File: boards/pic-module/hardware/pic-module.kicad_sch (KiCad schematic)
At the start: 42 parts, among them J2 ICSP, J20 12V IN, J3 J3 host, J4 J4 host, J5 UART, Q1 SUD50P04-08, U1 PIC32MK1024MCM064-I/PT, U2 MCP1826S-3302E/DB, U20 TDN 5-2411WI, Y1 12MHz

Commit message: Move core, can-card, io-card, serial-card, can-ssr, probe-helper to rev B
Rev A went to PCBWay and is tagged revA. Rev B replaces parts the Mouser
BOM check flagged (obsolete, end of life, not recommended for new designs,
or not orderable) and swaps out-of-stock passives and diodes for in-stock
equivalents. Field-only changes, same footprints, no layout change; the
reference boards (can-controller, pic-module) get the same part numbers.
The rev A order lists (DigiKey, Mouser) carry the same substitutions; the
Mouser list leaves out the T821 box headers (bought from DigiKey).

docs/rev-b-changes.md lists every change and the rev B to-dos (MAX7219 is
obsolete and must be replaced). transfer/mouser-revA.xlsx (Mouser BOM
check) consumed.

Co-Authored-By: Claude Opus 5.5 <noreply@anthropic.com>
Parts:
- C1, C2, C60, C61, C62, C63, C8: MPN GRM31CR71E106KA12L -> CL31B106KAHNNNE; Manufacturer Murata -> Samsung Electro-Mechanics
- C10: MPN GRM31MR71H105KA88L -> C1206C105K5RACTU; Manufacturer Murata -> KEMET
- C11, C12: MPN GRM2165C1H270JA01D -> C0805C270J5GACTU; Manufacturer Murata -> KEMET
- C13, C3, C4, C5, C6, C7, C9: MPN GRM21BR71H104KA01L -> C0805C104K5RACTU; Manufacturer Murata -> KEMET
- D1, D2, D32: MPN LTST-C150GKT -> LTST-C150KGKT
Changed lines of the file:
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@@
 			)
 		)
-		(property "Manufacturer" "Murata"
+		(property "Manufacturer" "Samsung Electro-Mechanics"
 			(at 142.24 68.58 0)
 			(hide yes)
@@
 			)
 		)
-		(property "MPN" "GRM31CR71E106KA12L"
+		(property "MPN" "CL31B106KAHNNNE"
 			(at 142.24 68.58 0)
 			(hide yes)
@@
 			)
 		)
-		(property "Manufacturer" "Murata"
+		(property "Manufacturer" "Samsung Electro-Mechanics"
 			(at 154.94 68.58 0)
 			(hide yes)
@@
 			)
 		)
-		(property "MPN" "GRM31CR71E106KA12L"
+		(property "MPN" "CL31B106KAHNNNE"
 			(at 154.94 68.58 0)
 			(hide yes)
@@
 			)
 		)
-		(property "MPN" "LTST-C150GKT"
+		(property "MPN" "LTST-C150KGKT"
 			(at 180.34 60.96 0)
 			(hide yes)
@@
 			)
 		)
-		(property "Manufacturer" "Murata"
+		(property "Manufacturer" "Samsung Electro-Mechanics"
 			(at 205.74 73.66 0)
 			(hide yes)
@@
 			)
 		)
-		(property "MPN" "GRM31CR71E106KA12L"
+		(property "MPN" "CL31B106KAHNNNE"
 			(at 205.74 73.66 0)
 			(hide yes)
@@
 			)
 		)
-		(property "Manufacturer" "Murata"
+		(property "Manufacturer" "Samsung Electro-Mechanics"
 			(at 254 73.66 0)
 			(hide yes)
@@
 			)
 		)
-		(property "MPN" "GRM31CR71E106KA12L"
+		(property "MPN" "CL31B106KAHNNNE"
 			(at 254 73.66 0)
 			(hide yes)
@@
 			)
 		)
-		(property "Manufacturer" "Murata"
+		(property "Manufacturer" "Samsung Electro-Mechanics"
 			(at 297.18 71.12 0)
 			(hide yes)
@@
 			)
 		)
-		(property "MPN" "GRM31CR71E106KA12L"
+		(property "MPN" "CL31B106KAHNNNE"
 			(at 297.18 71.12 0)
 			(hide yes)
@@
 			)
 		)
-		(property "Manufacturer" "Murata"
+		(property "Manufacturer" "Samsung Electro-Mechanics"
 			(at 335.28 71.12 0)
 			(hide yes)
@@
 			)
 		)
-		(property "MPN" "GRM31CR71E106KA12L"
+		(property "MPN" "CL31B106KAHNNNE"
 			(at 335.28 71.12 0)
 			(hide yes)
@@
 			)
 		)
-		(property "MPN" "LTST-C150GKT"
+		(property "MPN" "LTST-C150KGKT"
 			(at 360.68 60.96 0)
 			(hide yes)
@@
 			)
 		)
-		(property "Manufacturer" "Murata"
+		(property "Manufacturer" "KEMET"
 			(at 25.4 129.54 0)
 			(hide yes)
@@
 			)
 		)
-		(property "MPN" "GRM21BR71H104KA01L"
+		(property "MPN" "C0805C104K5RACTU"
 			(at 25.4 129.54 0)
 			(hide yes)
@@
 			)
 		)
-		(property "Manufacturer" "Murata"
+		(property "Manufacturer" "KEMET"
 			(at 40.64 129.54 0)
 			(hide yes)
@@
 			)
 		)
-		(property "MPN" "GRM21BR71H104KA01L"
+		(property "MPN" "C0805C104K5RACTU"
 			(at 40.64 129.54 0)
 			(hide yes)
@@
 			)
 		)
-		(property "Manufacturer" "Murata"
+		(property "Manufacturer" "KEMET"
 			(at 55.88 129.54 0)
 			(hide yes)
@@
 			)
 		)
-		(property "MPN" "GRM21BR71H104KA01L"
+		(property "MPN" "C0805C104K5RACTU"
 			(at 55.88 129.54 0)
 			(hide yes)
@@
 			)
 		)
-		(property "Manufacturer" "Murata"
+		(property "Manufacturer" "KEMET"
 			(at 71.12 129.54 0)
 			(hide yes)
@@
 			)
 		)
-		(property "MPN" "GRM21BR71H104KA01L"
+		(property "MPN" "C0805C104K5RACTU"
 			(at 71.12 129.54 0)
 			(hide yes)
@@
 			)
 		)
-		(property "Manufacturer" "Murata"
+		(property "Manufacturer" "KEMET"
 			(at 86.36 129.54 0)
 			(hide yes)
@@
 			)
 		)
-		(property "MPN" "GRM21BR71H104KA01L"
+		(property "MPN" "C0805C104K5RACTU"
 			(at 86.36 129.54 0)
 			(hide yes)
@@
 			)
 		)
-		(property "Manufacturer" "Murata"
+		(property "Manufacturer" "Samsung Electro-Mechanics"
 			(at 101.6 129.54 0)
 			(hide yes)
@@
 			)
 		)
-		(property "MPN" "GRM31CR71E106KA12L"
+		(property "MPN" "CL31B106KAHNNNE"
 			(at 101.6 129.54 0)
 			(hide yes)
@@
 			)
 		)
-		(property "Manufacturer" "Murata"
+		(property "Manufacturer" "KEMET"
 			(at 45.72 165.1 0)
 			(hide yes)
@@
 			)
 		)
-		(property "MPN" "GRM21BR71H104KA01L"
+		(property "MPN" "C0805C104K5RACTU"
 			(at 45.72 165.1 0)
 			(hide yes)
@@
 			)
 		)
-		(property "Manufacturer" "Murata"
+		(property "Manufacturer" "KEMET"
 			(at 58.42 165.1 0)
 			(hide yes)
@@
 			)
 		)
-		(property "MPN" "GRM31MR71H105KA88L"
+		(property "MPN" "C1206C105K5RACTU"
 			(at 58.42 165.1 0)
 			(hide yes)
@@
 			)
 		)
-		(property "Manufacturer" "Murata"
+		(property "Manufacturer" "KEMET"
 			(at 35.56 215.9 0)
 			(hide yes)
@@
 			)
 		)
-		(property "MPN" "GRM2165C1H270JA01D"
+		(property "MPN" "C0805C270J5GACTU"
 			(at 35.56 215.9 0)
 			(hide yes)
@@
 			)
 		)
-		(property "Manufacturer" "Murata"
+		(property "Manufacturer" "KEMET"
 			(at 55.88 215.9 0)
 			(hide yes)
@@
 			)
 		)
-		(property "MPN" "GRM2165C1H270JA01D"
+		(property "MPN" "C0805C270J5GACTU"
 			(at 55.88 215.9 0)
 			(hide yes)
@@
 			)
 		)
-		(property "Manufacturer" "Murata"
+		(property "Manufacturer" "KEMET"
 			(at 43.18 256.54 0)
 			(hide yes)
@@
 			)
 		)
-		(property "MPN" "GRM21BR71H104KA01L"
+		(property "MPN" "C0805C104K5RACTU"
 			(at 43.18 256.54 0)
 			(hide yes)
@@
 			)
 		)
-		(property "MPN" "LTST-C150GKT"
+		(property "MPN" "LTST-C150KGKT"
 			(at 254 238.76 0)
 			(hide yes)

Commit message: Rev B / rev A order: 10 uF CL31B106KAHZW6E, beads BLM31PG391SN1L
Both earlier substitutes (CL31B106KAHNNNE, BLM31KN102SH1L) are on
backorder at Mouser. CL31B106KAHZW6E has the same rating (1.4 mm tall).
The isolated-supply beads need no 1 kOhm: TI's reference uses 330 Ohm;
BLM31PG391SN1L is 390 Ohm @ 100 MHz, 2 A, 50 mOhm. Field-only changes;
order lists regenerated.

Co-Authored-By: Claude Opus 5.5 <noreply@anthropic.com>
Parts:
- C1, C2, C60, C61, C62, C63, C8: MPN CL31B106KAHNNNE -> CL31B106KAHZW6E
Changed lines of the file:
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@@
 			)
 		)
-		(property "MPN" "CL31B106KAHNNNE"
+		(property "MPN" "CL31B106KAHZW6E"
 			(at 142.24 68.58 0)
 			(hide yes)
@@
 			)
 		)
-		(property "MPN" "CL31B106KAHNNNE"
+		(property "MPN" "CL31B106KAHZW6E"
 			(at 154.94 68.58 0)
 			(hide yes)
@@
 			)
 		)
-		(property "MPN" "CL31B106KAHNNNE"
+		(property "MPN" "CL31B106KAHZW6E"
 			(at 205.74 73.66 0)
 			(hide yes)
@@
 			)
 		)
-		(property "MPN" "CL31B106KAHNNNE"
+		(property "MPN" "CL31B106KAHZW6E"
 			(at 254 73.66 0)
 			(hide yes)
@@
 			)
 		)
-		(property "MPN" "CL31B106KAHNNNE"
+		(property "MPN" "CL31B106KAHZW6E"
 			(at 297.18 71.12 0)
 			(hide yes)
@@
 			)
 		)
-		(property "MPN" "CL31B106KAHNNNE"
+		(property "MPN" "CL31B106KAHZW6E"
 			(at 335.28 71.12 0)
 			(hide yes)
@@
 			)
 		)
-		(property "MPN" "CL31B106KAHNNNE"
+		(property "MPN" "CL31B106KAHZW6E"
 			(at 101.6 129.54 0)
 			(hide yes)

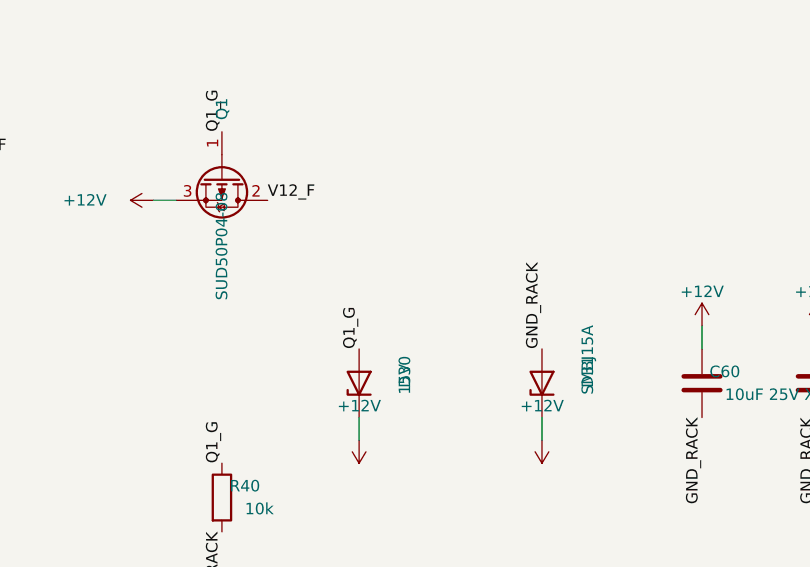
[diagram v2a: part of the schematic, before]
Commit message: Mouser cart: SQD50P04-09L P-FET, Diotec P6SMBJ15A TVS
Out of stock: Vishay SUD50P04-08-GE3 (core Q1) -> SQD50P04-09L_GE3 and
Littelfuse SMBJ15A (12 V input TVS) -> Diotec P6SMBJ15A, same footprints,
in core, can-ssr and the can-controller/pic-module references. Logged in
docs/rev-b-changes.md; order lists regenerated. The cart as ordered is
docs/orders/mouser-cart-2026-10-12.xls.

Co-Authored-By: Claude Opus 5.5 <noreply@anthropic.com>
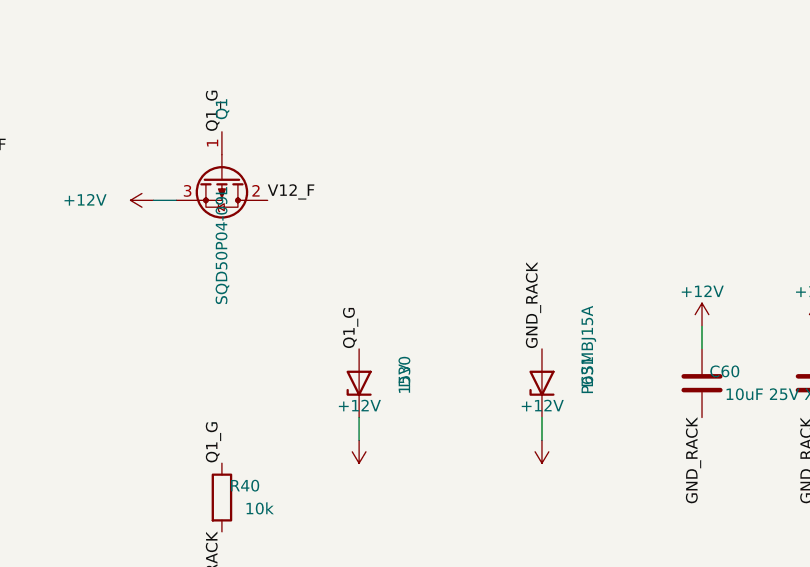
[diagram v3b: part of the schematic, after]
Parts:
- D31: value SMBJ15A -> P6SMBJ15A; MPN SMBJ15A -> P6SMBJ15A; Manufacturer Littelfuse -> Diotec Semiconductor
- Q1: value SUD50P04-08 -> SQD50P04-09L; MPN SUD50P04-08-GE3 -> SQD50P04-09L_GE3
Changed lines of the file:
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@@
 			)
 		)
-		(property "Value" "SUD50P04-08"
+		(property "Value" "SQD50P04-09L"
 			(at 88.9 53.34 0)
 			(effects
@@
 			)
 		)
-		(property "MPN" "SUD50P04-08-GE3"
+		(property "MPN" "SQD50P04-09L_GE3"
 			(at 88.9 45.72 0)
 			(hide yes)
@@
 			)
 		)
-		(property "Value" "SMBJ15A"
+		(property "Value" "P6SMBJ15A"
 			(at 129.54 69.85 0)
 			(effects
@@
 			)
 		)
-		(property "Manufacturer" "Littelfuse"
+		(property "Manufacturer" "Diotec Semiconductor"
 			(at 124.46 68.58 0)
 			(hide yes)
@@
 			)
 		)
-		(property "MPN" "SMBJ15A"
+		(property "MPN" "P6SMBJ15A"
 			(at 124.46 68.58 0)
 			(hide yes)
